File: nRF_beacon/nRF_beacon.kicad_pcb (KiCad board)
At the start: 4 copper layers, 53 parts, among them J1 Conn_02x05_Odd_Even, J2 Conn_02x03_Counter_Clockwise, U1 nRF54L15-QFAA, U2 NPM1300-QEAA-R7, U3 MAX98357A, U4 12BHC186P1-GR, X1 32MHz, X2 32.768 kHz

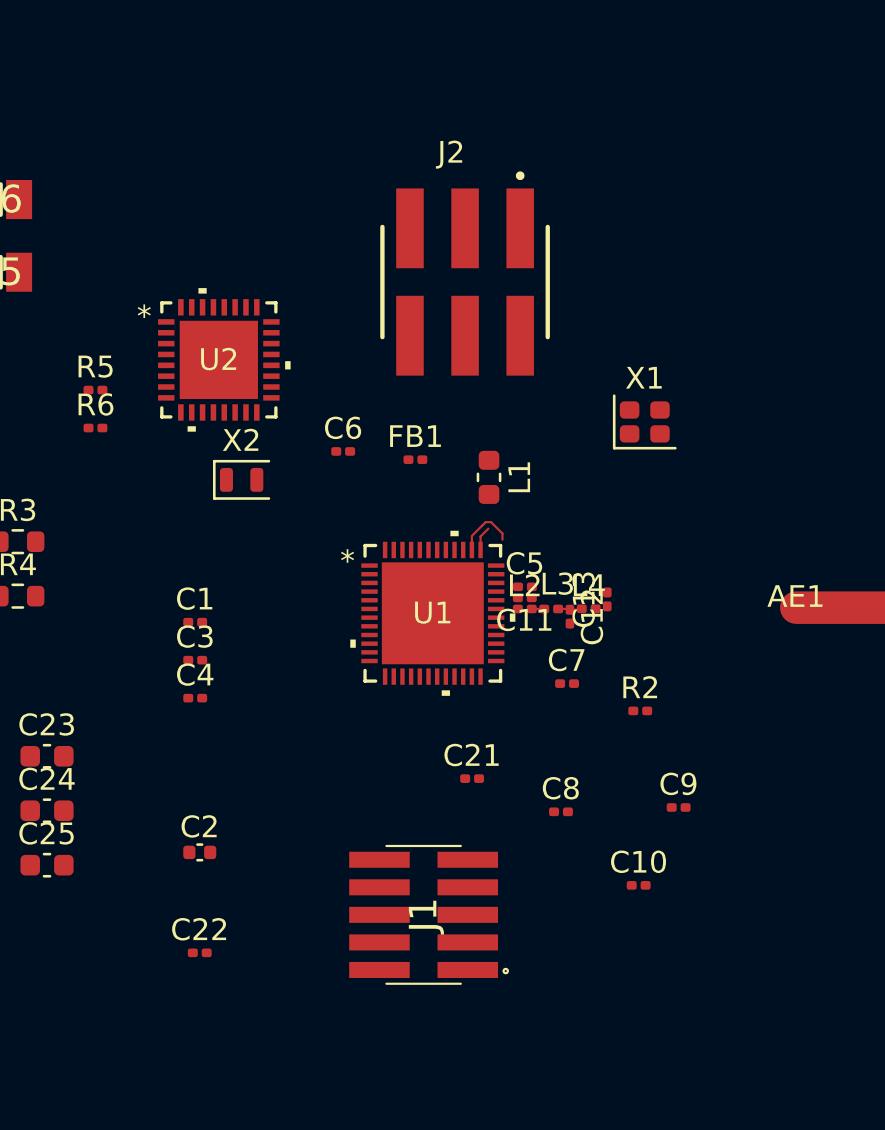
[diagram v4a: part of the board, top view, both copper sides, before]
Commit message: Added most of the components to nRF54 typical application layout
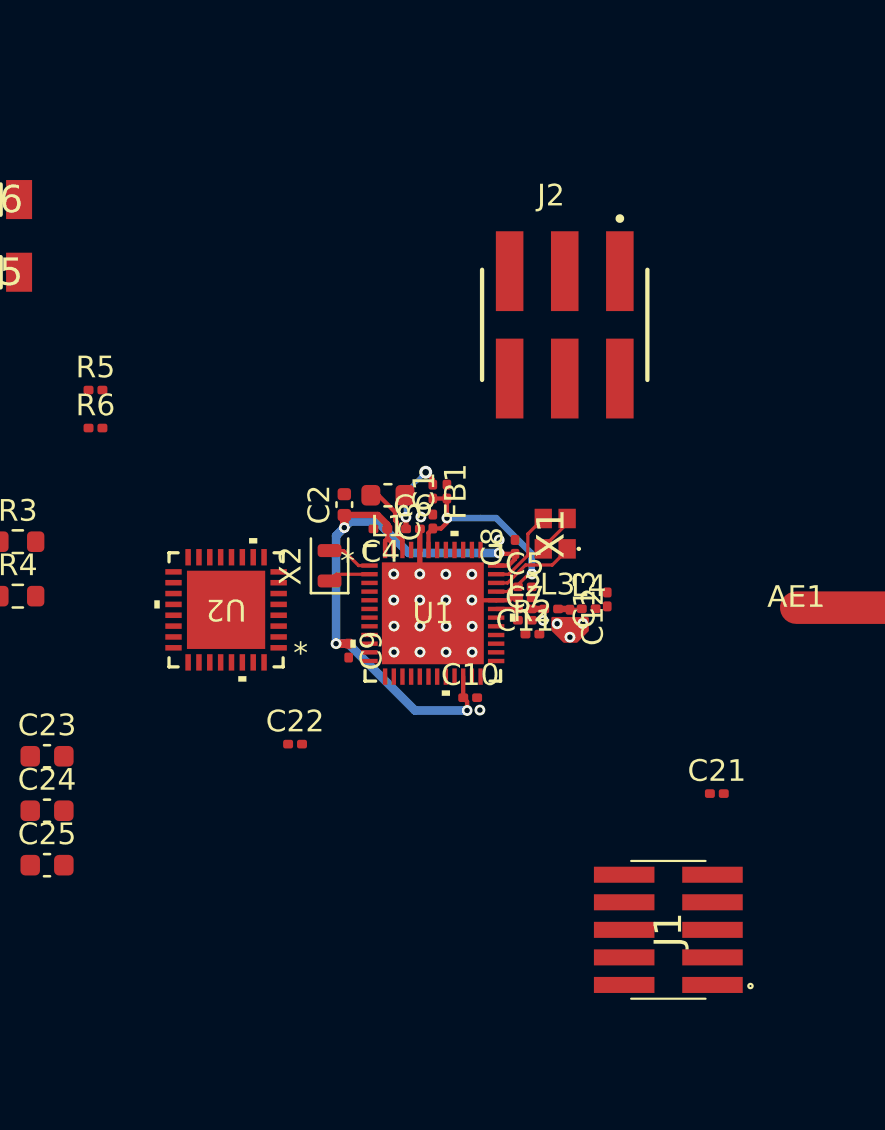
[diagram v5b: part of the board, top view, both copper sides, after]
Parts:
- X1: footprint Crystal:Crystal_SMD_2016-4Pin_2.0x1.6mm -> Ekse:CX2016DB32000D0WZRC1
- moved C2 17.4 mm to (167.1, 56.2), turned to 90 degrees
- moved C9 16.8 mm to (167.3, 62.9), turned to -90 degrees
- moved C1 13.1 mm to (171.8, 55.6), turned to 90 degrees
- moved C3 12.7 mm to (171.2, 57.0), turned to 90 degrees
- moved C8 12.4 mm to (175.0, 58.1), turned to 90 degrees
- moved C10 11.6 mm to (172.9, 65.1)
- moved C4 11.6 mm to (168.8, 57.3), turned to 180 degrees
- moved U2 11.5 mm to (161.7, 61.0), turned to 180 degrees
- moved C21 11.3 mm to (184.3, 69.5)
- moved J1 11.3 mm to (182.0, 75.8)
- moved C22 10.6 mm to (164.8, 67.2)
- moved X1 6.60 mm to (176.8, 57.5), turned to 90 degrees
- moved R2 6.10 mm to (175.8, 62.2)
- moved X2 5.67 mm to (166.4, 59.0), turned to 90 degrees
- moved J2 5.00 mm to (177.3, 47.9)
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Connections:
- C1 pad 2: Earth -> GND
- C10 pad 2: Earth -> GND
- C11 pad 2: Earth -> GND
- C12 pad 2: Earth -> GND
- C13 pad 2: Earth -> GND
- C15 pad 2: Earth -> GND
- C17 pad 2: Earth -> GND
- C18 pad 2: Earth -> GND
- C19 pad 2: Earth -> GND
- C2 pad 2: Earth -> GND
- C20 pad 2: Earth -> GND
- C21 pad 2: Earth -> GND
- C22 pad 2: Earth -> GND
- C25 pad 2: Earth -> GND
- C3 pad 2: Earth -> GND
- C4 pad 2: Earth -> GND
- C5 pad 2: Earth -> GND
- C6 pad 2: Earth -> GND
- C7 pad 2: Earth -> GND
- C8 pad 2: Earth -> GND
- C9 pad 2: Earth -> GND
- J1 pad 3: Earth -> GND
- J1 pad 5: Earth -> GND
- J1 pad 9: Earth -> GND
- NT1 pad 2: Earth -> GND
- NT2 pad 2: Earth -> GND
- R5 pad 1: Earth -> GND
- R6 pad 1: Earth -> GND
- U1 pad 32: Earth -> GND
- U1 pad 44: Earth -> GND
- U1 pad 49: Earth -> GND
- U2 pad 33: Earth -> GND
- U3 pad 11: Earth -> GND
- U3 pad 15: Earth -> GND
- U3 pad 17: Earth -> GND
- U3 pad 2: Earth -> GND
- U3 pad 3: Earth -> GND
- U4 pad 2: Earth -> GND
- X1 pad 1: /MCU/XC2 -> /MCU/XC1
- X1 pad 2: /MCU/XC1 -> GND
- X1 pad 3: (no net) -> /MCU/XC2
- X1 pad 4: (no net) -> GND
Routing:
- net VDD_nRF: track 0.00 -> 29.5 mm, vias 0 -> 4
- net Net-(U1A-DECA): track 0.00 -> 11.2 mm, vias 0 -> 2
- net GND: track 0.00 -> 10.2 mm, vias 0 -> 23
- net /MCU/XC1: track 0.00 -> 3.96 mm
- net /MCU/XC2: track 0.00 -> 3.81 mm
- net Net-(U1A-DECD): track 0.00 -> 3.70 mm, vias 0 -> 2
- net Net-(U1A-DCC): track 0.00 -> 3.32 mm
- net /P1.10: track 2.82 -> 0.00 mm
- net Net-(U1C-P1.00/XL1): track 0.00 -> 2.13 mm
- net Net-(U1C-P1.01/XL2): track 0.00 -> 1.97 mm
- net /P1.09: track 1.13 -> 0.00 mm
- net Net-(U1A-ANT): track 0.00 -> 1.00 mm

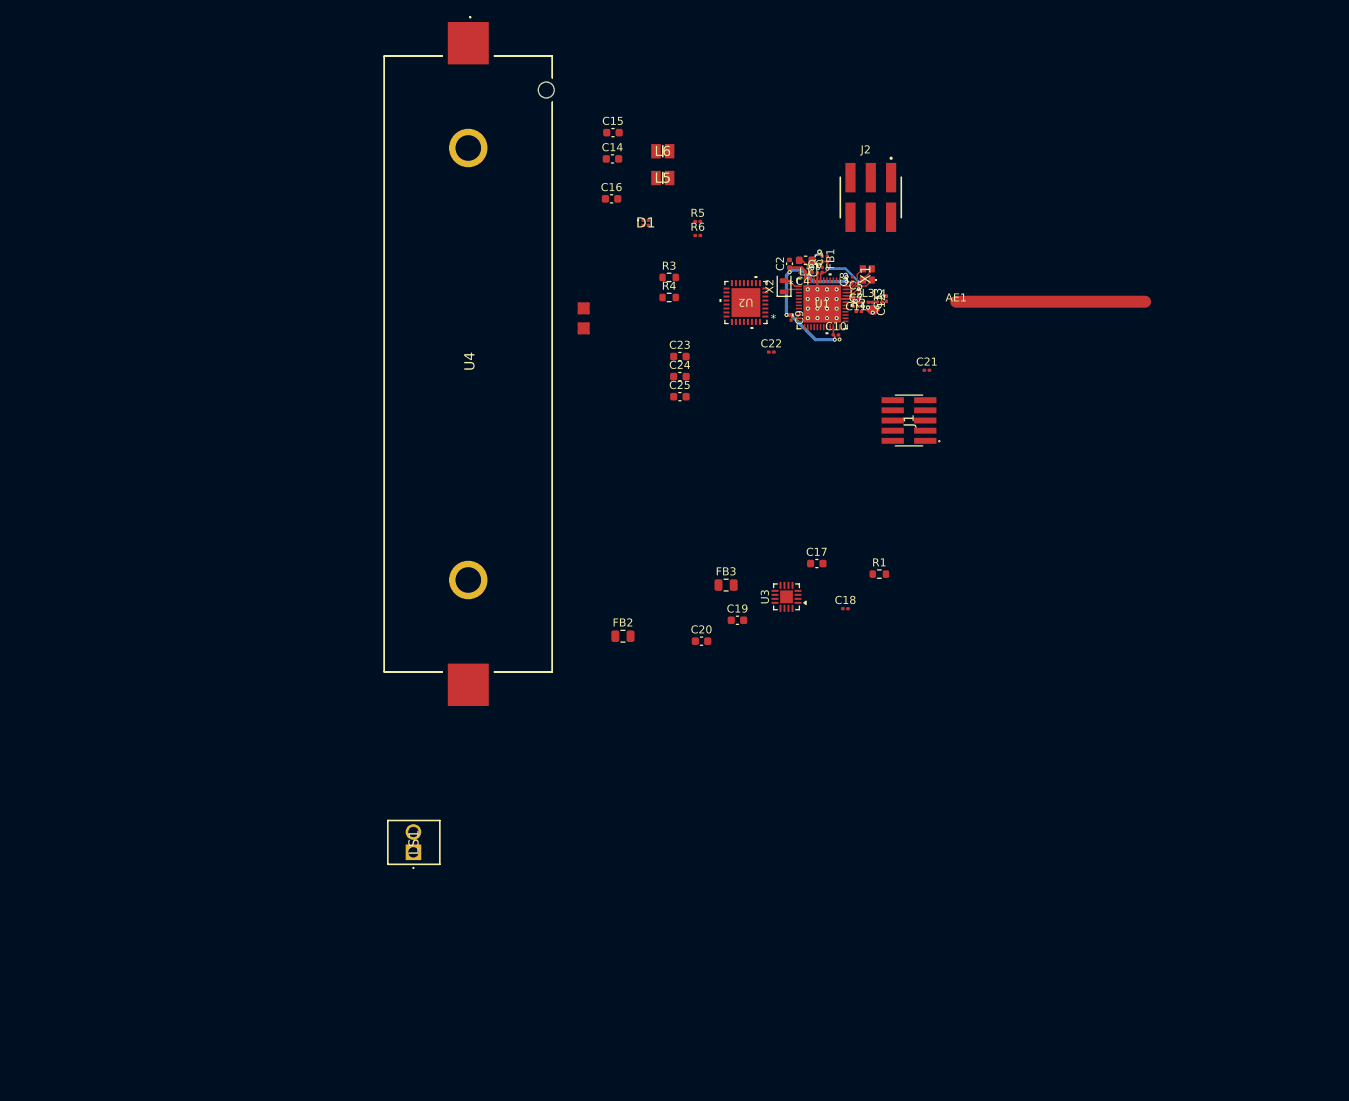
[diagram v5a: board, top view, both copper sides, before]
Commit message: Adjusted antenna layout
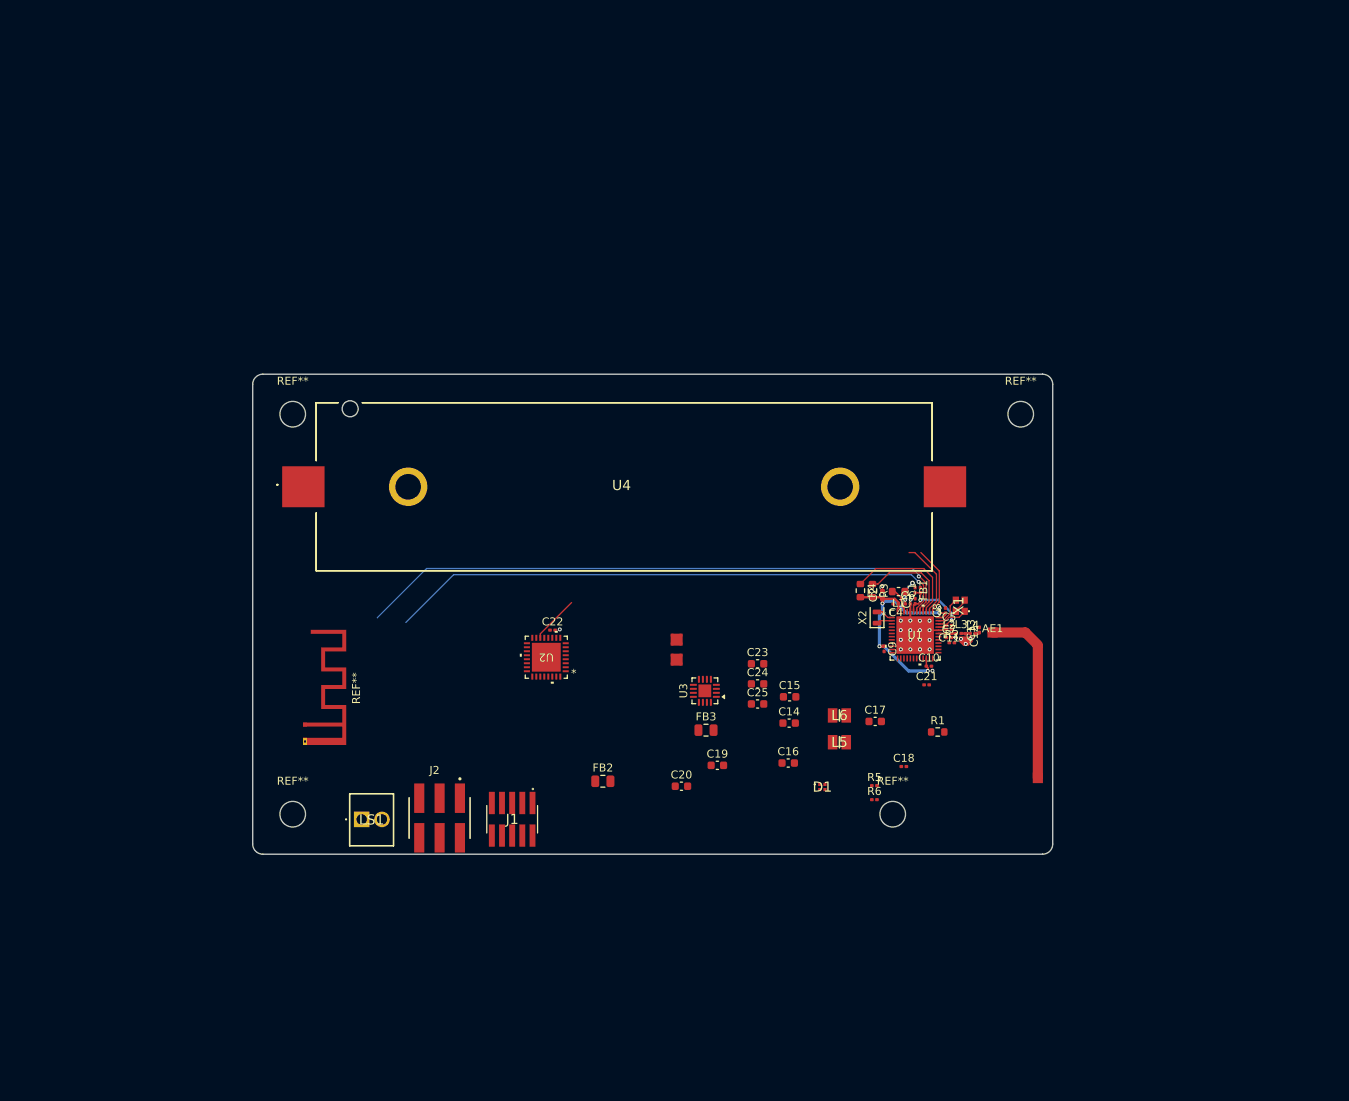
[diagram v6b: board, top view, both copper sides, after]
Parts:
- added REF**: MountingHole_3.2mm_M3, MountingHole:MountingHole_3.2mm_M3, F.Cu at (105.0, 75.0)
- added REF**: MountingHole_3.2mm_M3, MountingHole:MountingHole_3.2mm_M3, F.Cu at (105.0, 125.0)
- added REF**: MountingHole_3.2mm_M3, MountingHole:MountingHole_3.2mm_M3, F.Cu at (196.0, 75.0)
- added REF**: Texas_SWRA117D_2.4GHz_Left, RF_Antenna:Texas_SWRA117D_2.4GHz_Left, F.Cu at (106.5, 113.8)
- added REF**: MountingHole_3.2mm_M3, MountingHole:MountingHole_3.2mm_M3, F.Cu at (180.0, 125.0)
- moved J2 94.5 mm to (123.4, 125.5)
- moved C15 73.9 mm to (167.1, 110.3)
- moved C16 73.9 mm to (166.9, 118.6)
- moved L5 73.9 mm to (173.3, 116.0)
- moved L6 73.9 mm to (173.3, 112.7)
- moved R5 73.9 mm to (177.7, 121.4)
- moved R6 73.9 mm to (177.7, 123.2)
- moved C14 73.9 mm to (167.1, 113.6)
- moved D1 73.9 mm to (171.2, 121.6)
- moved J1 70.3 mm to (132.4, 125.6), turned to 180 degrees
- moved U2 50.9 mm to (136.7, 105.4)
- moved R3 46.7 mm to (177.5, 97.0), turned to -90 degrees
- moved C22 44.2 mm to (137.5, 102.0)
- moved R4 43.8 mm to (176.0, 97.0), turned to -90 degrees
- moved NT2 43.0 mm to (153.0, 105.7)
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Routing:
- net /P1.13: track 0.00 -> 75.9 mm, vias 0 -> 1
- net /P1.14: track 0.00 -> 71.4 mm, vias 0 -> 1
- net /MCU/SCL: track 0.00 -> 18.5 mm
- net /MCU/SDA: track 0.00 -> 14.9 mm
- net /P1.10: track 0.00 -> 9.59 mm
- net /P1.09: track 0.00 -> 8.69 mm
- net VDD_nRF: track 29.5 -> 32.3 mm
- net GND: track 10.2 -> 11.4 mm, vias 23 -> 25
- net /MCU/RF: track 0.00 -> 0.58 mm
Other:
- board outline added: 100 x 60 mm

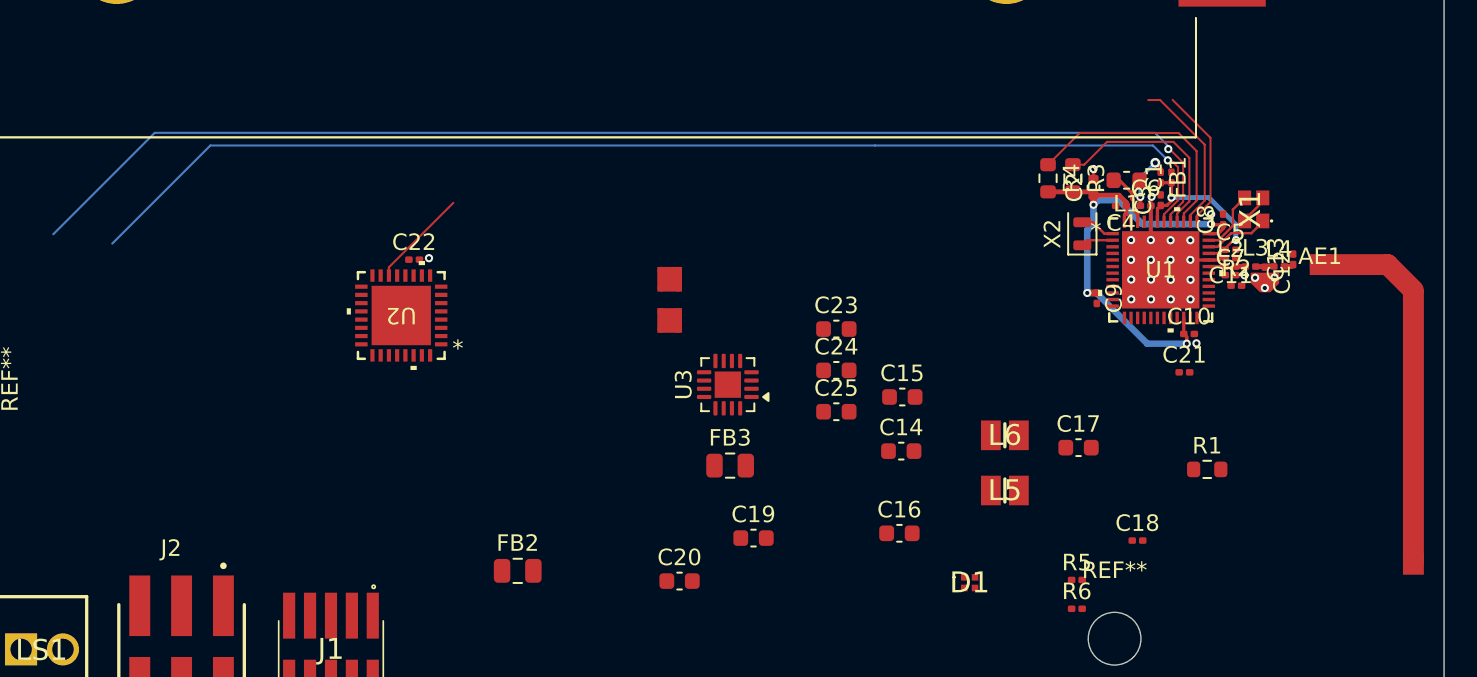
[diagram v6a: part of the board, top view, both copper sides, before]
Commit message: Added transmission line, and new folder for report screenshots
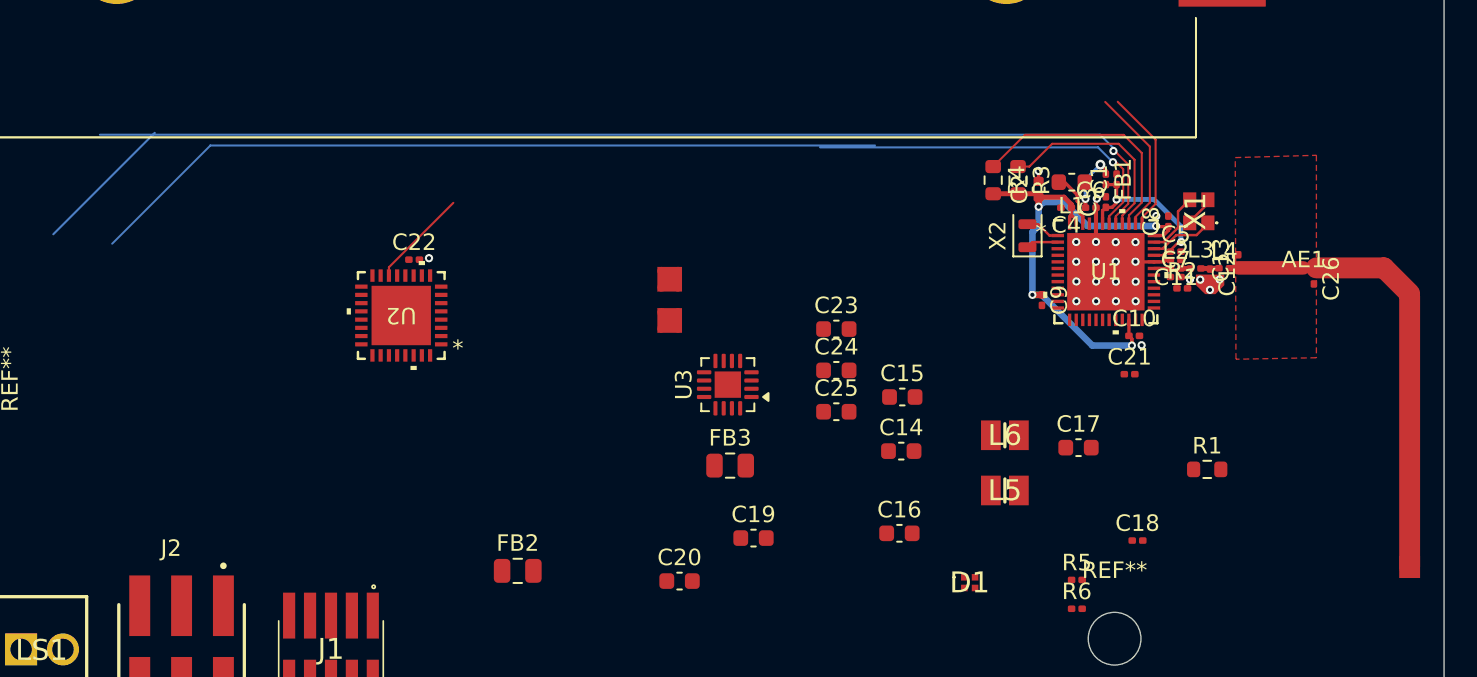
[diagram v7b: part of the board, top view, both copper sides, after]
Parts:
- added C26: 1.4pF, Capacitor_SMD:C_0201_0603Metric, F.Cu at (192.1, 103.1)
- moved C13 3.33 mm to (187.5, 102.0)
- moved C2 3.33 mm to (175.4, 97.7)
- moved C3 3.33 mm to (179.5, 98.5)
- moved C8 3.33 mm to (183.3, 99.7)
- moved R3 3.33 mm to (174.1, 97.2)
- moved R4 3.33 mm to (172.6, 97.2)
- moved U1 3.33 mm to (179.5, 102.7)
- moved C10 3.33 mm to (181.2, 106.6)
- moved C12 3.33 mm to (185.8, 102.9)
- moved C21 3.33 mm to (180.9, 108.9)
- moved FB1 3.33 mm to (179.5, 97.1)
- moved L4 3.33 mm to (186.7, 102.5)
- moved L2 3.33 mm to (183.7, 102.5)
- moved L3 3.33 mm to (184.9, 102.5)
- moved X1 3.33 mm to (185.1, 99.1)
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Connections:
- X1 pad 2: GND -> (no net)
- X1 pad 4: GND -> (no net)
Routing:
- net /MCU/RF: track 0.58 -> 3.95 mm
- net /P1.10: track 9.59 -> 8.87 mm
- added copper zone on F.Cu, net GND
